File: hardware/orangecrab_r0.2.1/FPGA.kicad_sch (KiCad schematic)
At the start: 14 parts, among them J6 Conn_01x05, U3 LFE5U-25F-8MG285C, U6 W25Q128JVP

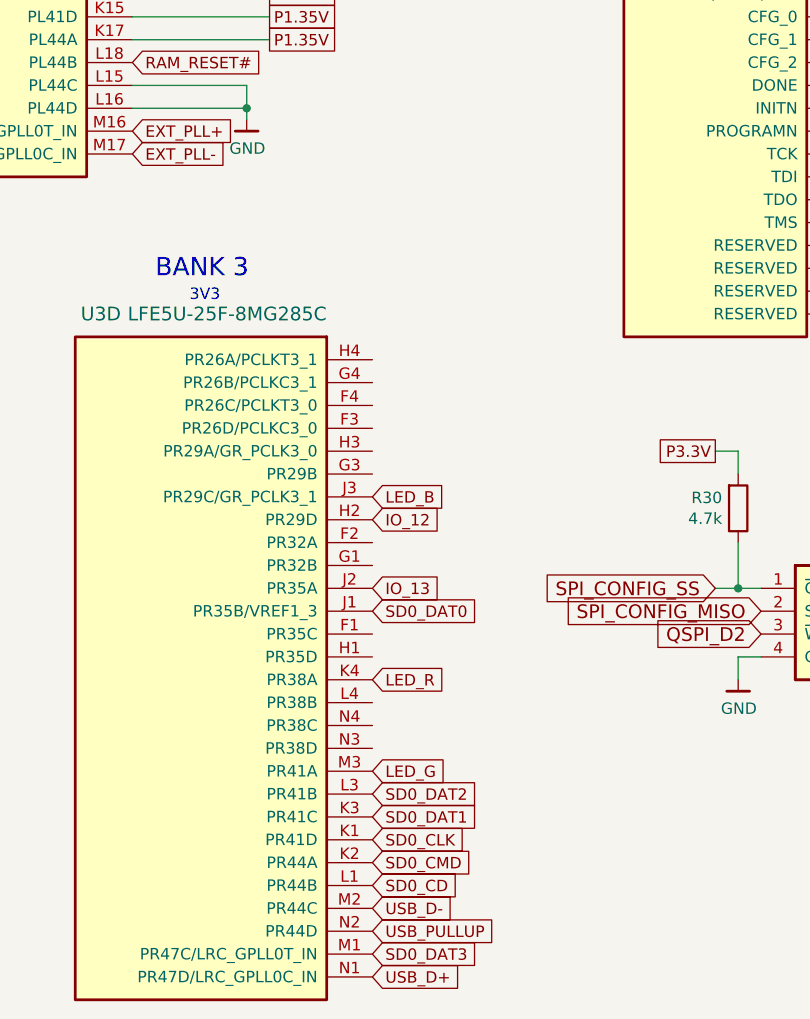
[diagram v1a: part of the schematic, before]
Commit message: delete redundant sheets
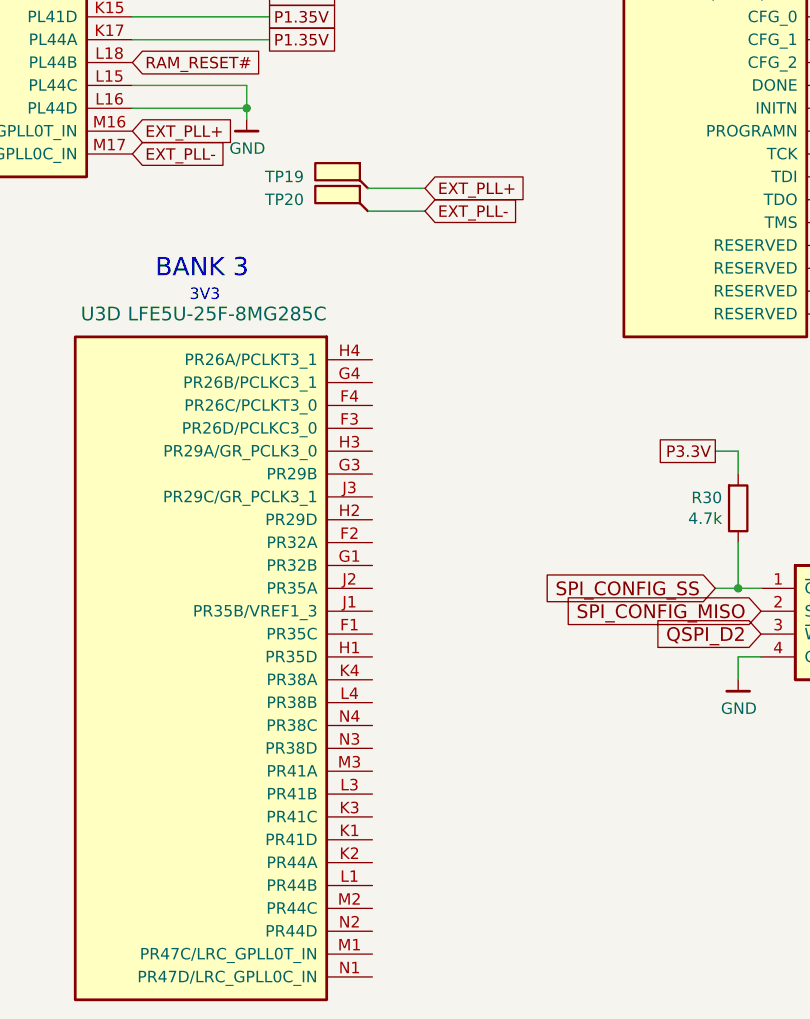
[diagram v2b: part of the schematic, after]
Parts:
- added TP19, TP20: SMD_TP, gkl_misc:TestPoint_Pad_D0.5mm, symbol Connector:TestPoint_Flag
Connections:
- net EXT_PLL+: now also TP19.1
- net EXT_PLL-: now also TP20.1
- net IO_12: no longer names the net of U3.H2 (PR29D)
- net IO_13: no longer names the net of U3.J2 (PR35A)
- net LED_B: no longer names the net of U3.J3 (PR29C/GR_PCLK3_1)
- net LED_G: no longer names the net of U3.M3 (PR41A)
- net LED_R: no longer names the net of U3.K4 (PR38A)
- net SD0_CD: no longer names the net of U3.L1 (PR44B)
- net SD0_CLK: no longer names the net of U3.K1 (PR41D)
- net SD0_CMD: no longer names the net of U3.K2 (PR44A)
- net SD0_DAT0: no longer names the net of U3.J1 (PR35B/VREF1_3)
- net SD0_DAT1: no longer names the net of U3.K3 (PR41C)
- net SD0_DAT2: no longer names the net of U3.L3 (PR41B)
- net SD0_DAT3: no longer names the net of U3.M1 (PR47C/LRC_GPLL0T_IN)
- net USB_D+: no longer names the net of U3.N1 (PR47D/LRC_GPLL0C_IN)
- net USB_D-: no longer names the net of U3.M2 (PR44C)
- net USB_PULLUP: no longer names the net of U3.N2 (PR44D)
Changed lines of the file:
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@@
     (stroke (width 0) (type default))
   )
+  (wire (pts (xy 150.622 100.33) (xy 144.272 100.33))
+    (stroke (width 0) (type default))
+  )
   (wire (pts (xy 64.77 113.03) (xy 67.31 113.03))
     (stroke (width 0) (type default))
@@
     (stroke (width 0) (type default))
   )
+  (wire (pts (xy 150.622 102.87) (xy 144.272 102.87))
+    (stroke (width 0) (type default))
+  )
   (wire (pts (xy 118.11 91.44) (xy 130.81 91.44))
     (stroke (width 0) (type default))
@@
     )
   )
-  (global_label "SD0_CMD" (shape input) (at 144.78 175.26 0)
-    (effects (font (size 1.27 1.27)) (justify left))
-    (property "Intersheetrefs" "${INTERSHEET_REFS}" (at 144.78 175.26 0)
-      (effects (font (size 1.27 1.27)) hide)
-    )
-  )
-  (global_label "SD0_DAT2" (shape input) (at 144.78 167.64 0)
-    (effects (font (size 1.27 1.27)) (justify left))
-    (property "Intersheetrefs" "${INTERSHEET_REFS}" (at 144.78 167.64 0)
-      (effects (font (size 1.27 1.27)) hide)
-    )
-  )
   (global_label "P1.35V" (shape passive) (at 250.19 129.54 180)
     (effects (font (size 1.27 1.27)) (justify right))
@@
     )
   )
-  (global_label "SD0_CLK" (shape input) (at 144.78 172.72 0)
-    (effects (font (size 1.27 1.27)) (justify left))
-    (property "Intersheetrefs" "${INTERSHEET_REFS}" (at 144.78 172.72 0)
-      (effects (font (size 1.27 1.27)) hide)
-    )
-  )
   (global_label "RAM_D9" (shape input) (at 118.11 45.72 0)
     (effects (font (size 1.27 1.27)) (justify left))
@@
     )
   )
-  (global_label "LED_B" (shape input) (at 144.78 134.62 0)
-    (effects (font (size 1.27 1.27)) (justify left))
-    (property "Intersheetrefs" "${INTERSHEET_REFS}" (at 144.78 134.62 0)
-      (effects (font (size 1.27 1.27)) hide)
-    )
-  )
   (global_label "P3.3V" (shape passive) (at 238.76 74.93 180)
     (effects (font (size 1.27 1.27)) (justify right))
@@
     )
   )
-  (global_label "USB_D+" (shape input) (at 144.78 187.96 0)
-    (effects (font (size 1.27 1.27)) (justify left))
-    (property "Intersheetrefs" "${INTERSHEET_REFS}" (at 144.78 187.96 0)
-      (effects (font (size 1.27 1.27)) hide)
-    )
-  )
   (global_label "RAM_BA2" (shape input) (at 50.8 46.99 0)
     (effects (font (size 1.27 1.27)) (justify left))
@@
     )
   )
+  (global_label "EXT_PLL-" (shape input) (at 150.622 102.87 0)
+    (effects (font (size 1.27 1.27)) (justify left))
+    (property "Intersheetrefs" "${INTERSHEET_REFS}" (at 150.622 102.87 0)
+      (effects (font (size 1.27 1.27)) hide)
+    )
+  )
   (global_label "RAM_D15" (shape input) (at 118.11 40.64 0)
     (effects (font (size 1.27 1.27)) (justify left))
@@
     )
   )
-  (global_label "SD0_DAT3" (shape input) (at 144.78 185.42 0)
-    (effects (font (size 1.27 1.27)) (justify left))
-    (property "Intersheetrefs" "${INTERSHEET_REFS}" (at 144.78 185.42 0)
-      (effects (font (size 1.27 1.27)) hide)
-    )
-  )
   (global_label "P1.35V" (shape passive) (at 133.35 81.28 0)
     (effects (font (size 1.27 1.27)) (justify left))
@@
     )
   )
-  (global_label "SD0_CD" (shape input) (at 144.78 177.8 0)
-    (effects (font (size 1.27 1.27)) (justify left))
-    (property "Intersheetrefs" "${INTERSHEET_REFS}" (at 144.78 177.8 0)
-      (effects (font (size 1.27 1.27)) hide)
-    )
-  )
   (global_label "QSPI_D2" (shape input) (at 187.96 149.86 180)
     (effects (font (size 1.524 1.524)) (justify right))
@@
     )
   )
+  (global_label "EXT_PLL+" (shape input) (at 150.622 100.33 0)
+    (effects (font (size 1.27 1.27)) (justify left))
+    (property "Intersheetrefs" "${INTERSHEET_REFS}" (at 150.622 100.33 0)
+      (effects (font (size 1.27 1.27)) hide)
+    )
+  )
   (global_label "RAM_A0" (shape input) (at 50.8 54.61 0)
     (effects (font (size 1.27 1.27)) (justify left))
@@
     )
   )
-  (global_label "LED_G" (shape input) (at 144.78 165.1 0)
-    (effects (font (size 1.27 1.27)) (justify left))
-    (property "Intersheetrefs" "${INTERSHEET_REFS}" (at 144.78 165.1 0)
-      (effects (font (size 1.27 1.27)) hide)
-    )
-  )
   (global_label "RAM_A4" (shape input) (at 50.8 49.53 0)
     (effects (font (size 1.27 1.27)) (justify left))
@@
     )
   )
-  (global_label "USB_D-" (shape input) (at 144.78 180.34 0)
-    (effects (font (size 1.27 1.27)) (justify left))
-    (property "Intersheetrefs" "${INTERSHEET_REFS}" (at 144.78 180.34 0)
-      (effects (font (size 1.27 1.27)) hide)
-    )
-  )
-  (global_label "USB_PULLUP" (shape input) (at 144.78 182.88 0)
-    (effects (font (size 1.27 1.27)) (justify left))
-    (property "Intersheetrefs" "${INTERSHEET_REFS}" (at 144.78 182.88 0)
-      (effects (font (size 1.27 1.27)) hide)
-    )
-  )
   (global_label "ECP5_VREF" (shape passive) (at 67.31 54.61 0)
     (effects (font (size 1.27 1.27)) (justify left))
@@
     )
   )
-  (global_label "SD0_DAT0" (shape input) (at 144.78 147.32 0)
-    (effects (font (size 1.27 1.27)) (justify left))
-    (property "Intersheetrefs" "${INTERSHEET_REFS}" (at 144.78 147.32 0)
-      (effects (font (size 1.27 1.27)) hide)
-    )
-  )
-  (global_label "LED_R" (shape input) (at 144.78 154.94 0)
-    (effects (font (size 1.27 1.27)) (justify left))
-    (property "Intersheetrefs" "${INTERSHEET_REFS}" (at 144.78 154.94 0)
-      (effects (font (size 1.27 1.27)) hide)
-    )
-  )
-  (global_label "SD0_DAT1" (shape input) (at 144.78 170.18 0)
-    (effects (font (size 1.27 1.27)) (justify left))
-    (property "Intersheetrefs" "${INTERSHEET_REFS}" (at 144.78 170.18 0)
-      (effects (font (size 1.27 1.27)) hide)
-    )
-  )
   (global_label "SPI_CONFIG_MISO" (shape input) (at 236.22 44.45 0)
     (effects (font (size 1.524 1.524)) (justify left))
@@
     )
   )
-  (global_label "IO_12" (shape input) (at 144.78 137.16 0)
-    (effects (font (size 1.27 1.27)) (justify left))
-    (property "Intersheetrefs" "${INTERSHEET_REFS}" (at 144.78 137.16 0)
-      (effects (font (size 1.27 1.27)) hide)
-    )
-  )
   (global_label "RAM_A12" (shape input) (at 50.8 41.91 0)
     (effects (font (size 1.27 1.27)) (justify left))
@@
     )
   )
-  (global_label "IO_13" (shape input) (at 144.78 144.78 0)
-    (effects (font (size 1.27 1.27)) (justify left))
-    (property "Intersheetrefs" "${INTERSHEET_REFS}" (at 144.78 144.78 0)
-      (effects (font (size 1.27 1.27)) hide)
-    )
-  )
   (global_label "RAM_D3" (shape input) (at 50.8 130.81 0)
     (effects (font (size 1.27 1.27)) (justify left))
@@
           (reference "#PWR0107") (unit 1)
         )
-        (path "/3fc0bb0e-dabc-4b81-bef6-ad7dd3f01477/00000000-0000-0000-0000-00005abc9a87"
-          (reference "#PWR?") (unit 1)
-        )
       )
     )
@@
           (reference "R27") (unit 1)
         )
-        (path "/3fc0bb0e-dabc-4b81-bef6-ad7dd3f01477/00000000-0000-0000-0000-00005abc9a87"
-          (reference "R?") (unit 1)
-        )
       )
     )
@@
           (reference "R31") (unit 1)
         )
-        (path "/3fc0bb0e-dabc-4b81-bef6-ad7dd3f01477/00000000-0000-0000-0000-00005abc9a87"
-          (reference "R?") (unit 1)
-        )
       )
     )
@@
           (reference "R30") (unit 1)
         )
-        (path "/3fc0bb0e-dabc-4b81-bef6-ad7dd3f01477/00000000-0000-0000-0000-00005abc9a87"
-          (reference "R?") (unit 1)
-        )
       )
     )
@@
           (reference "R39") (unit 1)
         )
-        (path "/3fc0bb0e-dabc-4b81-bef6-ad7dd3f01477/00000000-0000-0000-0000-00005abc9a87"
-          (reference "R?") (unit 1)
+      )
+    )
+  )
+  (symbol (lib_id "Connector:TestPoint_Flag") (at 144.272 102.87 0) (mirror y) (unit 1)
+    (in_bom yes) (on_board yes) (dnp no)
+    (property "Reference" "TP20" (at 132.842 101.6 0)
+      (effects (font (size 1.27 1.27)) (justify right))
+    )
+    (property "Value" "SMD_TP" (at 145.3896 102.7938 0)
+      (effects (font (size 1.27 1.27)) (justify right) hide)
+    )
+    (property "Footprint" "gkl_misc:TestPoint_Pad_D0.5mm" (at 139.192 102.87 0)
+      (effects (font (size 1.27 1.27)) hide)
+    )
+    (property "Datasheet" "~" (at 139.192 102.87 0)
+      (effects (font (size 1.27 1.27)) hide)
+    )
+    (property "PN" "DNP" (at 144.272 102.87 0)
+      (effects (font (size 1.27 1.27)) hide)
+    )
+    (pin "1")
+    (instances
+      (project "OrangeCrab"
+        (path "/3fc0bb0e-dabc-4b81-bef6-ad7dd3f01477/00000000-0000-0000-0000-00005ab8acb7"
+          (reference "TP20") (unit 1)
+        )
+      )
+    )
+  )
+  (symbol (lib_id "Connector:TestPoint_Flag") (at 144.272 100.33 0) (mirror y) (unit 1)
+    (in_bom yes) (on_board yes) (dnp no)
+    (property "Reference" "TP19" (at 132.842 99.06 0)
+      (effects (font (size 1.27 1.27)) (justify right))
+    )
+    (property "Value" "SMD_TP" (at 145.3896 100.2538 0)
+      (effects (font (size 1.27 1.27)) (justify right) hide)
+    )
+    (property "Footprint" "gkl_misc:TestPoint_Pad_D0.5mm" (at 139.192 100.33 0)
+      (effects (font (size 1.27 1.27)) hide)
+    )
+    (property "Datasheet" "~" (at 139.192 100.33 0)
+      (effects (font (size 1.27 1.27)) hide)
+    )
+    (property "PN" "DNP" (at 144.272 100.33 0)
+      (effects (font (size 1.27 1.27)) hide)
+    )
+    (pin "1")
+    (instances
+      (project "OrangeCrab"
+        (path "/3fc0bb0e-dabc-4b81-bef6-ad7dd3f01477/00000000-0000-0000-0000-00005ab8acb7"
+          (reference "TP19") (unit 1)
         )
       )

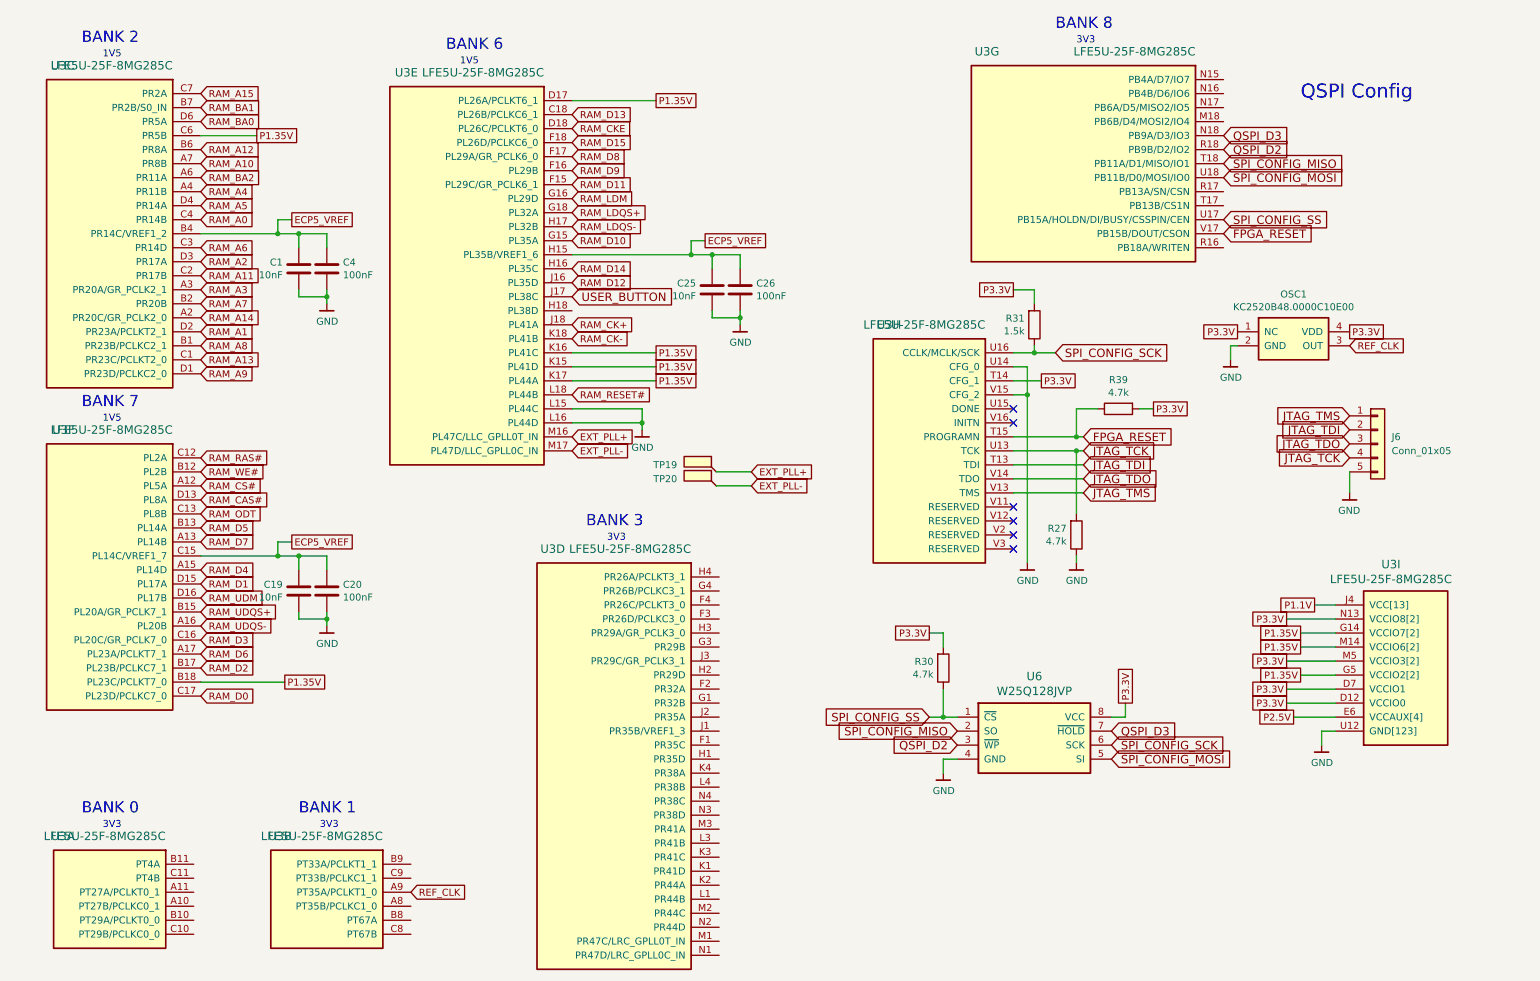
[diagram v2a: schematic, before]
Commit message: connect all spare IOs to M.2
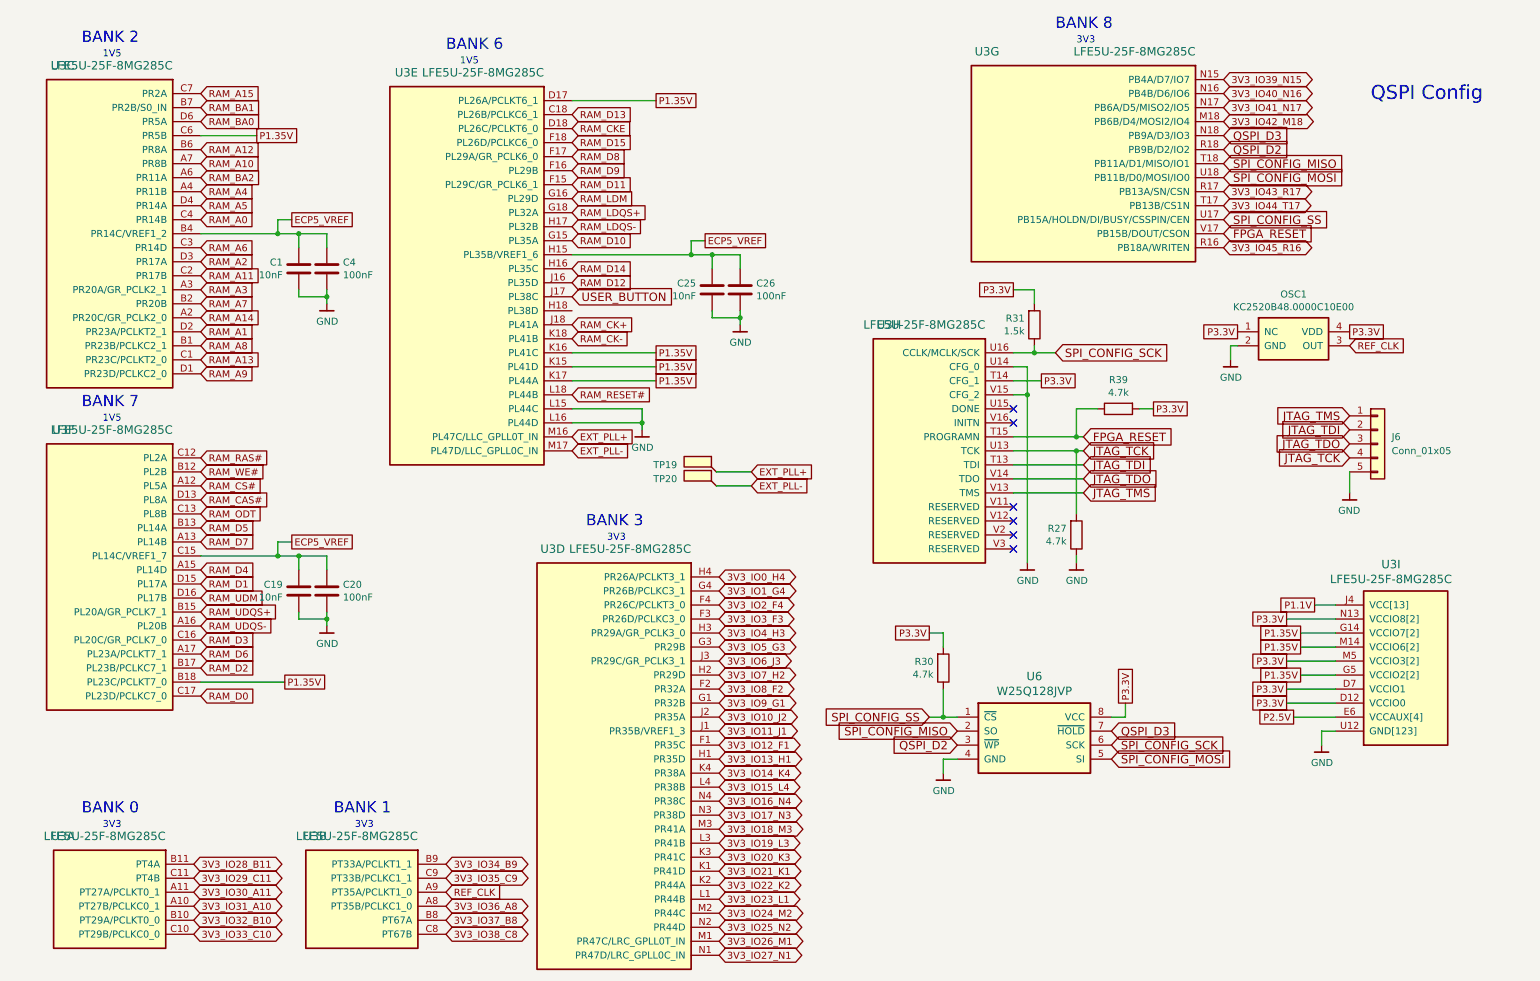
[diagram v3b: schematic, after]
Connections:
- net 3V3_IO31_A10: now reaches U3.A10 (PT27B/PCLKC0_1)
- net 3V3_IO30_A11: now reaches U3.A11 (PT27A/PCLKT0_1)
- net 3V3_IO32_B10: now reaches U3.B10 (PT29A/PCLKT0_0)
- net 3V3_IO28_B11: now reaches U3.B11 (PT4A)
- net 3V3_IO33_C10: now reaches U3.C10 (PT29B/PCLKC0_0)
- net 3V3_IO29_C11: now reaches U3.C11 (PT4B)
- net 3V3_IO36_A8: now reaches U3.A8 (PT35B/PCLKC1_0)
- net 3V3_IO37_B8: now reaches U3.B8 (PT67A)
- net 3V3_IO34_B9: now reaches U3.B9 (PT33A/PCLKT1_1)
- net 3V3_IO38_C8: now reaches U3.C8 (PT67B)
- net 3V3_IO35_C9: now reaches U3.C9 (PT33B/PCLKC1_1)
- net 3V3_IO12_F1: now reaches U3.F1 (PR35C)
- net 3V3_IO8_F2: now reaches U3.F2 (PR32A)
- net 3V3_IO3_F3: now reaches U3.F3 (PR26D/PCLKC3_0)
- net 3V3_IO2_F4: now reaches U3.F4 (PR26C/PCLKT3_0)
- net 3V3_IO9_G1: now reaches U3.G1 (PR32B)
- net 3V3_IO5_G3: now reaches U3.G3 (PR29B)
- net 3V3_IO1_G4: now reaches U3.G4 (PR26B/PCLKC3_1)
- net 3V3_IO13_H1: now reaches U3.H1 (PR35D)
- net 3V3_IO7_H2: now reaches U3.H2 (PR29D)
- net 3V3_IO4_H3: now reaches U3.H3 (PR29A/GR_PCLK3_0)
- net 3V3_IO0_H4: now reaches U3.H4 (PR26A/PCLKT3_1)
- net 3V3_IO11_J1: now reaches U3.J1 (PR35B/VREF1_3)
- net 3V3_IO10_J2: now reaches U3.J2 (PR35A)
- net 3V3_IO6_J3: now reaches U3.J3 (PR29C/GR_PCLK3_1)
- net 3V3_IO21_K1: now reaches U3.K1 (PR41D)
- net 3V3_IO22_K2: now reaches U3.K2 (PR44A)
- net 3V3_IO20_K3: now reaches U3.K3 (PR41C)
- net 3V3_IO14_K4: now reaches U3.K4 (PR38A)
- net 3V3_IO23_L1: now reaches U3.L1 (PR44B)
- net 3V3_IO19_L3: now reaches U3.L3 (PR41B)
- net 3V3_IO15_L4: now reaches U3.L4 (PR38B)
- net 3V3_IO26_M1: now reaches U3.M1 (PR47C/LRC_GPLL0T_IN)
- net 3V3_IO24_M2: now reaches U3.M2 (PR44C)
- net 3V3_IO18_M3: now reaches U3.M3 (PR41A)
- net 3V3_IO27_N1: now reaches U3.N1 (PR47D/LRC_GPLL0C_IN)
- net 3V3_IO25_N2: now reaches U3.N2 (PR44D)
- net 3V3_IO17_N3: now reaches U3.N3 (PR38D)
- net 3V3_IO16_N4: now reaches U3.N4 (PR38C)
- net 3V3_IO42_M18: now reaches U3.M18 (PB6B/D4/MOSI2/IO4)
- net 3V3_IO39_N15: now reaches U3.N15 (PB4A/D7/IO7)
- net 3V3_IO40_N16: now reaches U3.N16 (PB4B/D6/IO6)
- net 3V3_IO41_N17: now reaches U3.N17 (PB6A/D5/MISO2/IO5)
- net 3V3_IO45_R16: now reaches U3.R16 (PB18A/WRITEN)
- net 3V3_IO43_R17: now reaches U3.R17 (PB13A/SN/CSN)
- net 3V3_IO44_T17: now reaches U3.T17 (PB13B/CS1N)
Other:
- moved on the sheet: U3B
